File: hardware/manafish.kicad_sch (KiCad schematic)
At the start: 4 parts, among them J6 Battery, J8 USB_C_Receptacle_USB2.0_14P

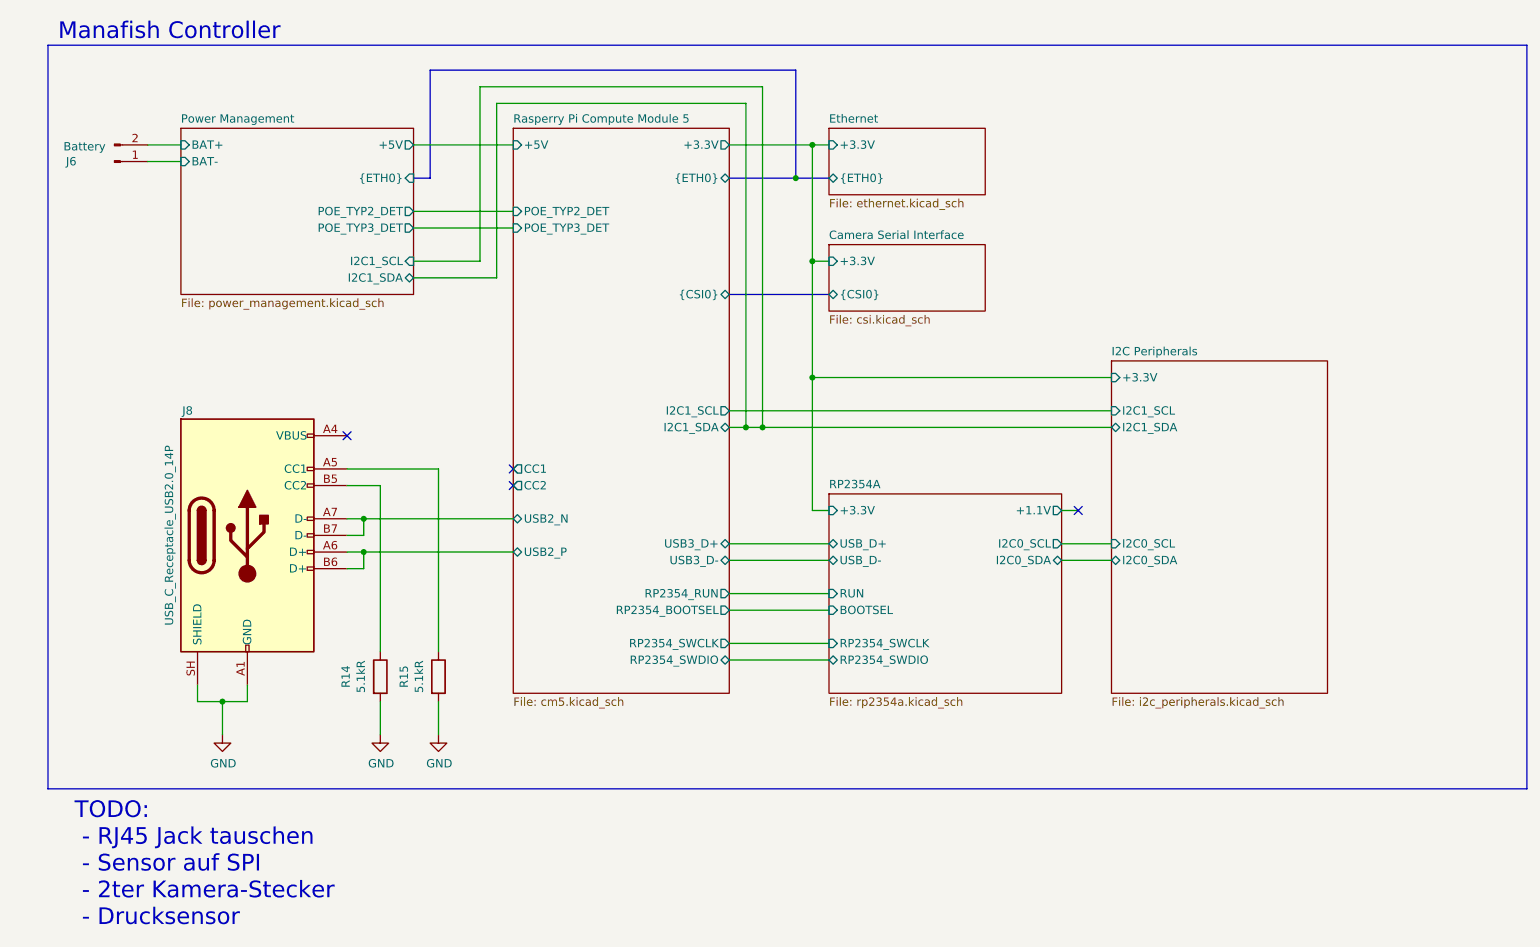
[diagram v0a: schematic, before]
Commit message: Feed +3.3V into the power management sheet
Replace the power management sheet's +5V output label with a +3.3V
input and wire the new sheet pin on the root schematic. Ignore KiCad's
local .history/ folder, which holds its own git repository.

Co-Authored-By: Claude Opus 5.5 <noreply@anthropic.com>
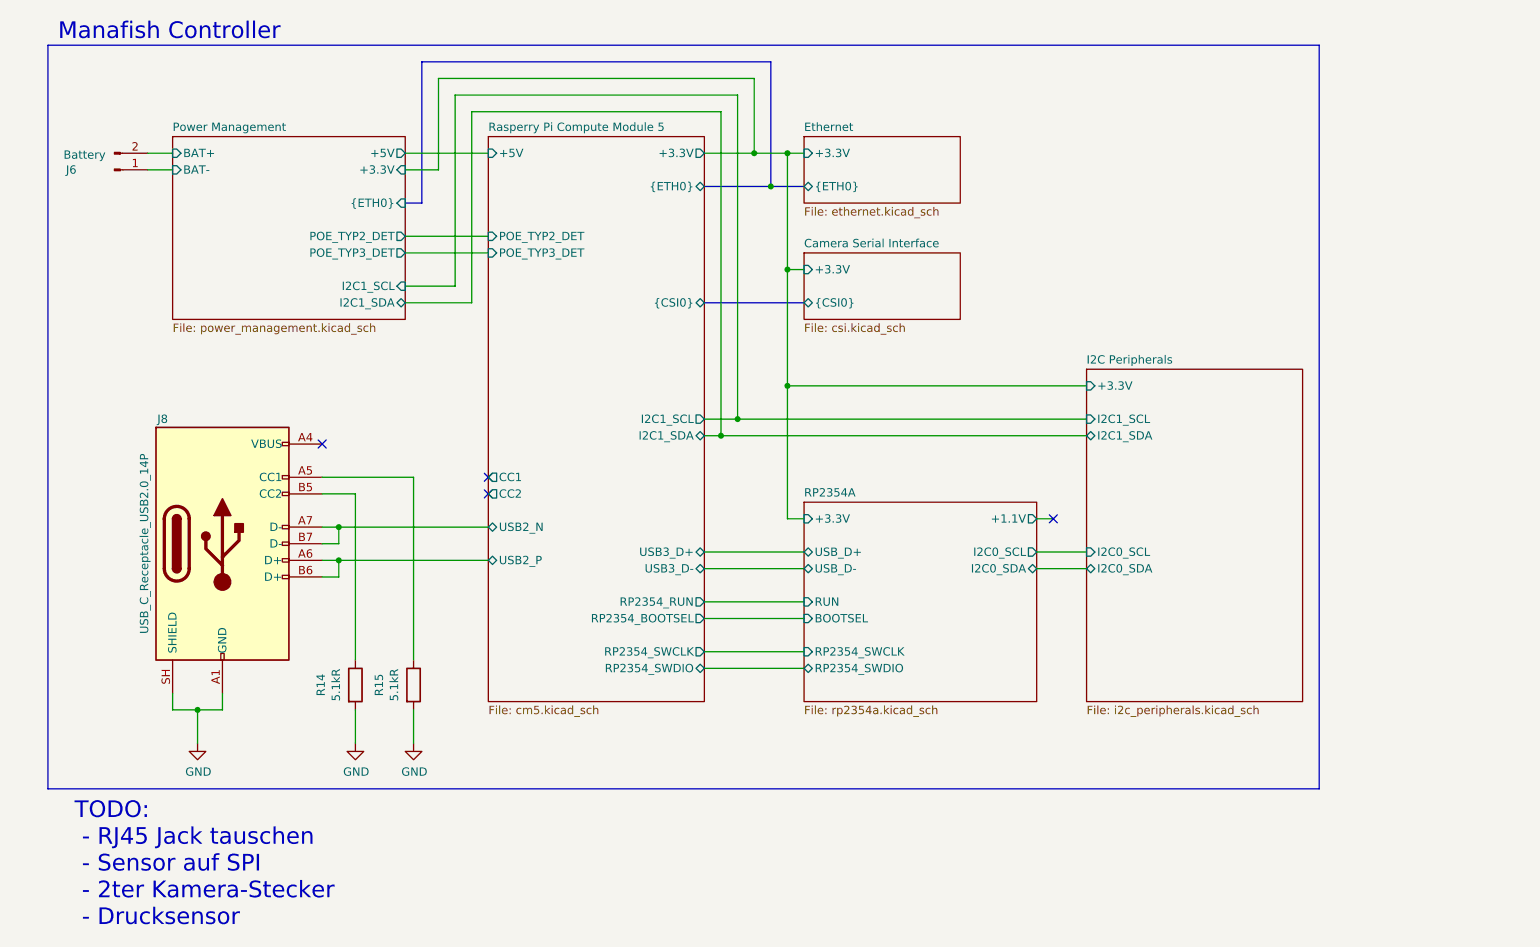
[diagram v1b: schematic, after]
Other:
- sheet Power Management ports: added +3.3V; removed none
- moved on the sheet: J6, J8, R14, R15
